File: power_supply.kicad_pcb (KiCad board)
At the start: 2 copper layers, 101.6 x 76.2 mm, 96 parts, among them J1 USB-IN, J2 USB OUT, Q1 SI4174DY, Q2 SI4463CDY, Q3 SI4463CDY, U1 LM3914, U10 FDC6392S, U11 MCP6041, U2 TPD2E001, U3 MIC2185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

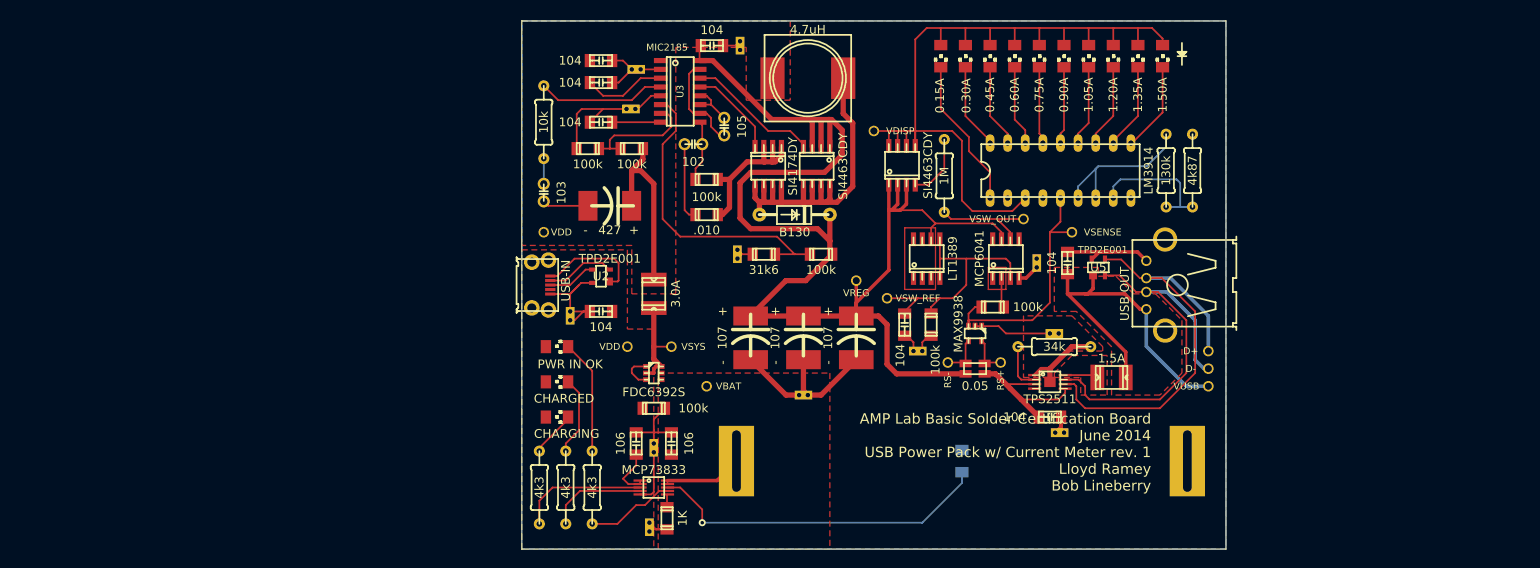
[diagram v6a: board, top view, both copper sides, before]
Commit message: Added silkscreen
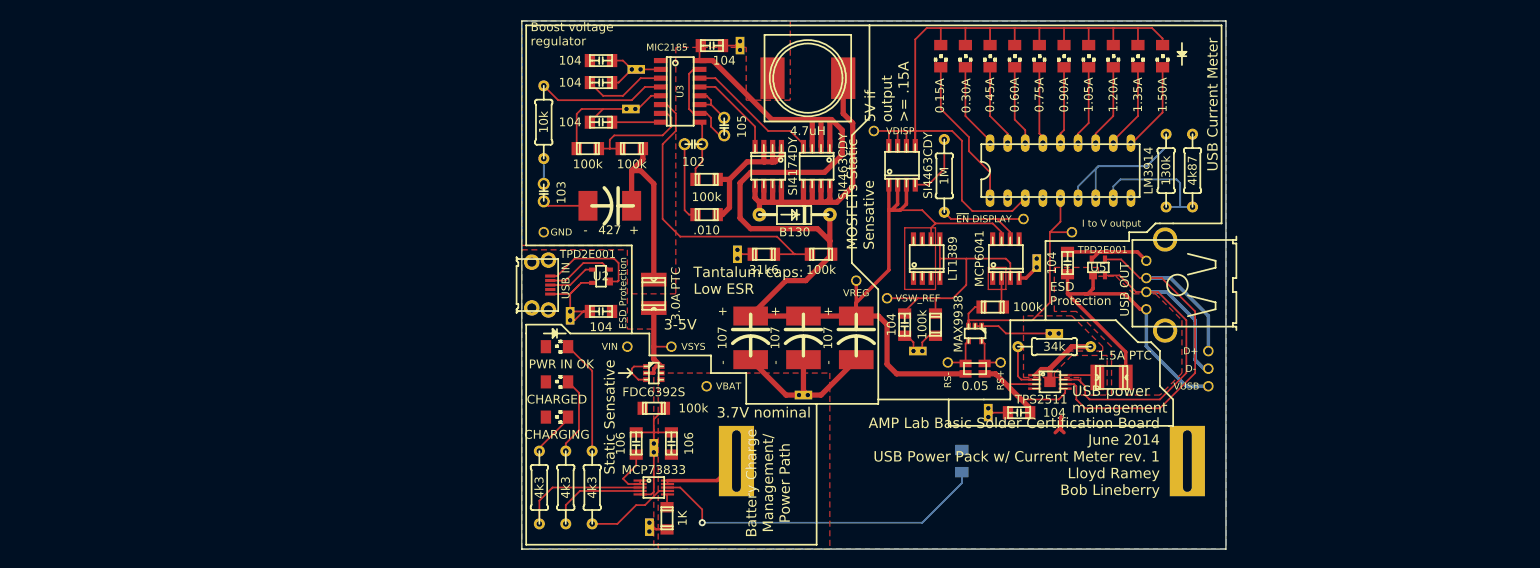
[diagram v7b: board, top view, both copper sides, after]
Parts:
- D11: value CHARGED -> CHARGED
- F1: value 3.0A -> 3.0A PTC
- F2: value 1.5A -> 1.5A PTC
- J1: value USB-IN -> USB IN
- TP1: value VDD -> VIN
- TP12: value VSW_OUT -> ~EN DISPLAY
- TP14: value VDD -> GND
- TP8: value VSENSE -> I to V output
- V12: value DBL_VIA -> DV
- moved V11 10.7 mm to (219.7, 158.1), turned to 90 degrees
- moved C11 4.49 mm to (224.2, 158.1), turned to 180 degrees
- moved R15 0.63 mm to (212.1, 145.4)
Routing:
- net (no net): track 0.00 -> 5.03 mm
- net /VOUT: track 23.0 -> 21.9 mm
- net N-0000042: track 39.9 -> 39.4 mm
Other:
- board text added: "3-5V"
- board text added: "3.7V nominal"
- board text added: "5V if output >= .15A"
- board text added: "Battery Charge Management/ Power Path"
- board text added: "Boost voltage regulator"
- board text added: "ESD Protection"
- board text added: "MOSFETs Static Sensative"
- board text added: "Static Sensative"
- board text added: "Tantalum caps: Low ESR"
- board text added: "USB Current Meter"
- board text added: "USB power management"

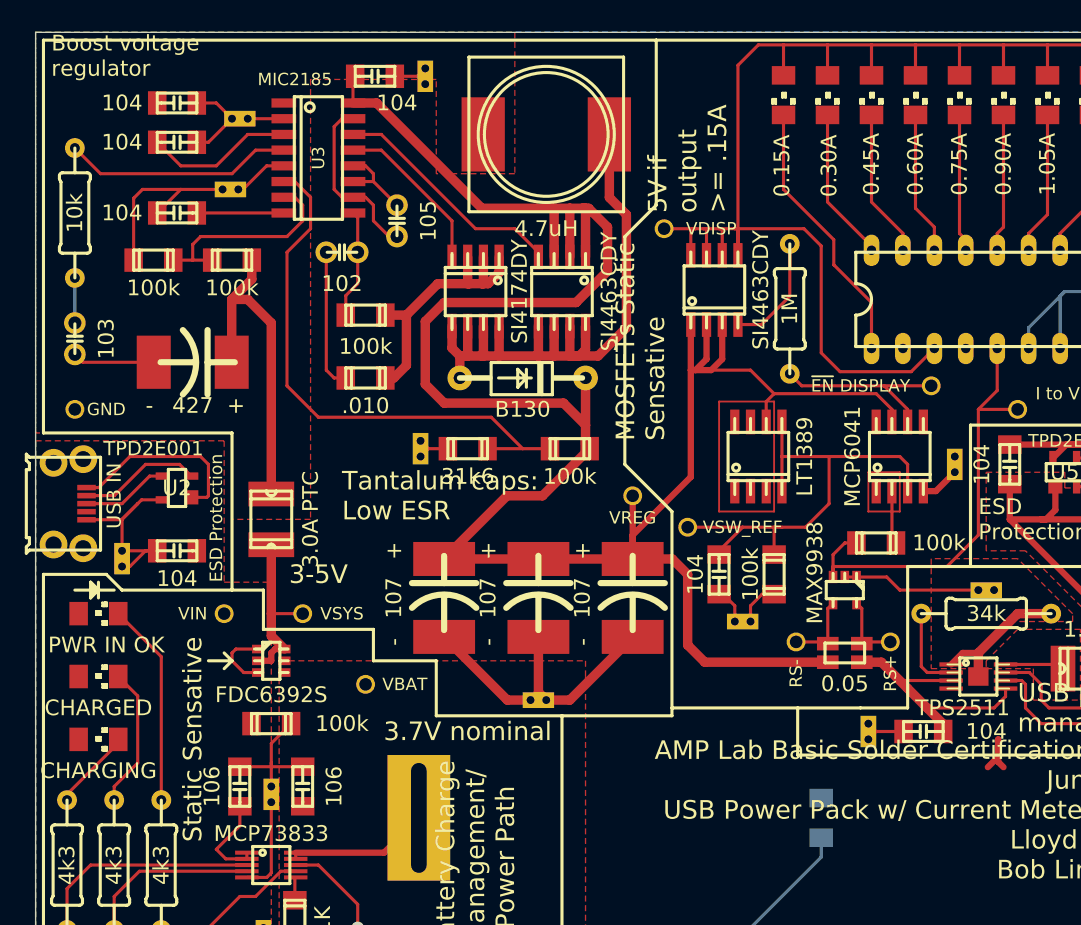
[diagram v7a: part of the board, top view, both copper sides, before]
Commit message: Updated silkscreen
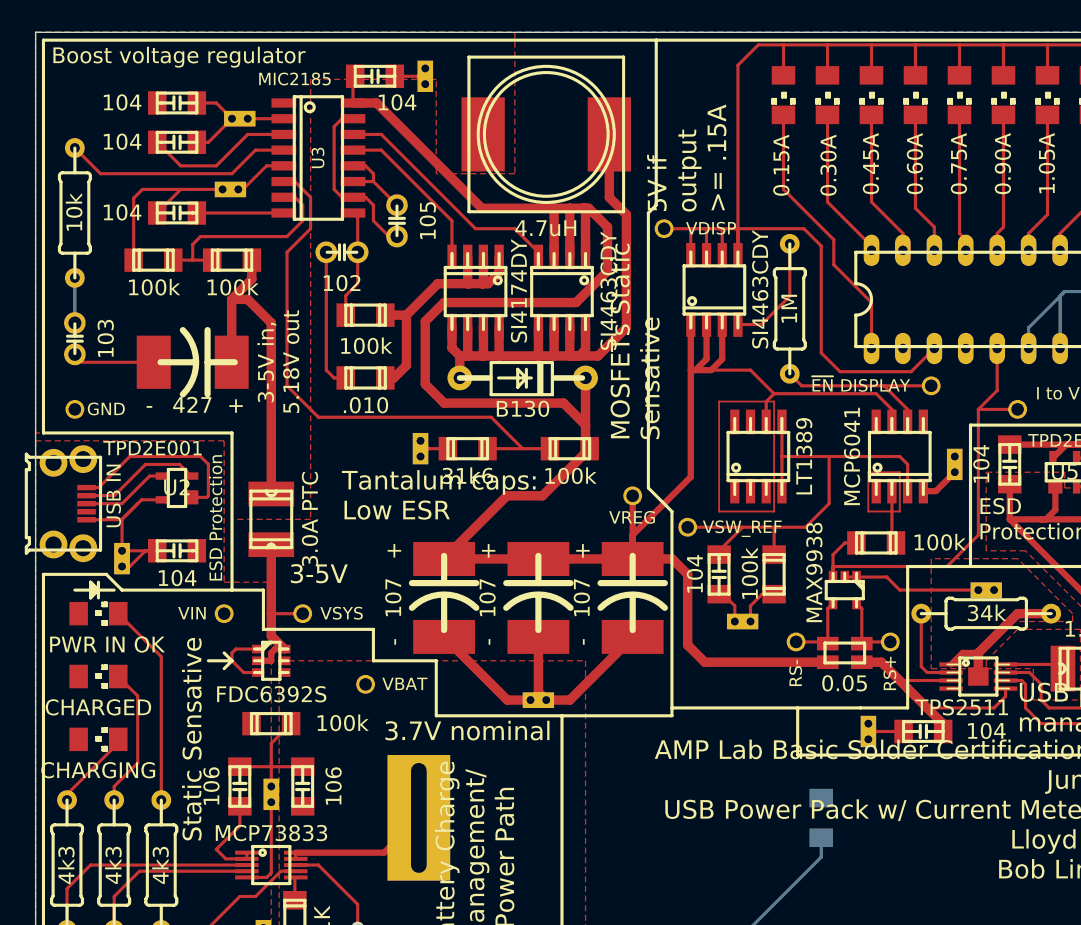
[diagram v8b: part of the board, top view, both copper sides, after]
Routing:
- net (no net): track 5.03 -> 0.00 mm
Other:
- board text added: "3-5V in, 5.18V out"
- board text added: "Battery Charge Management/Power Path: Controls Li-Ion charge profile (CC @ 1A -> CV @ 4.2V) Automatically switches between external and battery power"
- board text added: "Boost Voltage Regulator: 95% efficient boost from 3-5V input to 5.18V output. Uses tantalum caps to reduce power loss due to ESR."
- board text added: "ESD Protection: Protects against external ESD events"
- board text added: "USB Current Meter: Measures current being drawn through USB jack. Turns off LM3914 when current < 0.15A to save power. Divide I to V output by 1.25 to get current drawn through USB."
- board text added: "USB Power Management: Sets D+/D- voltage levels correctly so that USB devices will charge."
